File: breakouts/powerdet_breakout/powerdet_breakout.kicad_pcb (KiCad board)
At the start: 4 copper layers, 27.8 x 24 mm, 27 parts, among them P1 CONN_01X08, U1 CONN_SMA, U2 ADL5902, U3 CONN_SMA, U4 mounting_box

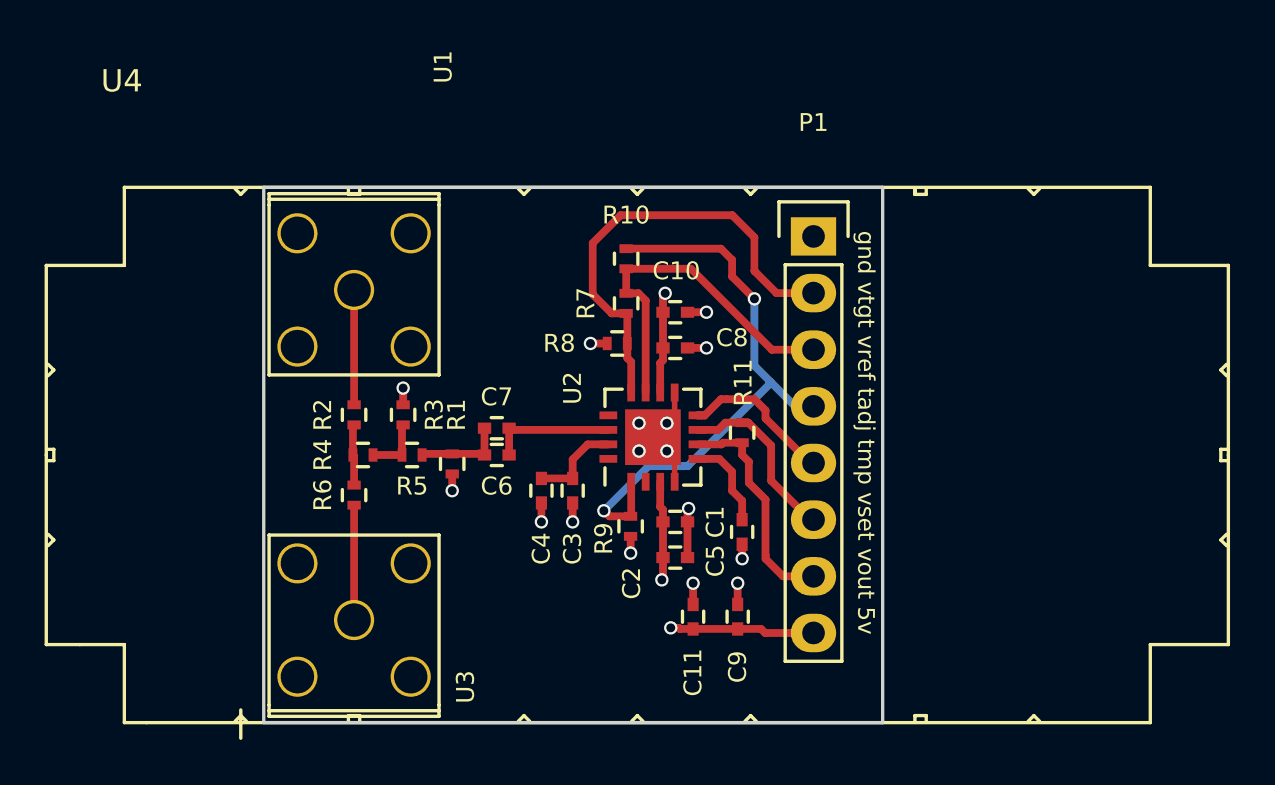
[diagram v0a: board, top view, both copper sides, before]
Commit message: trimmed ground plane on some breakouts so it doesn't disappear during panelization..
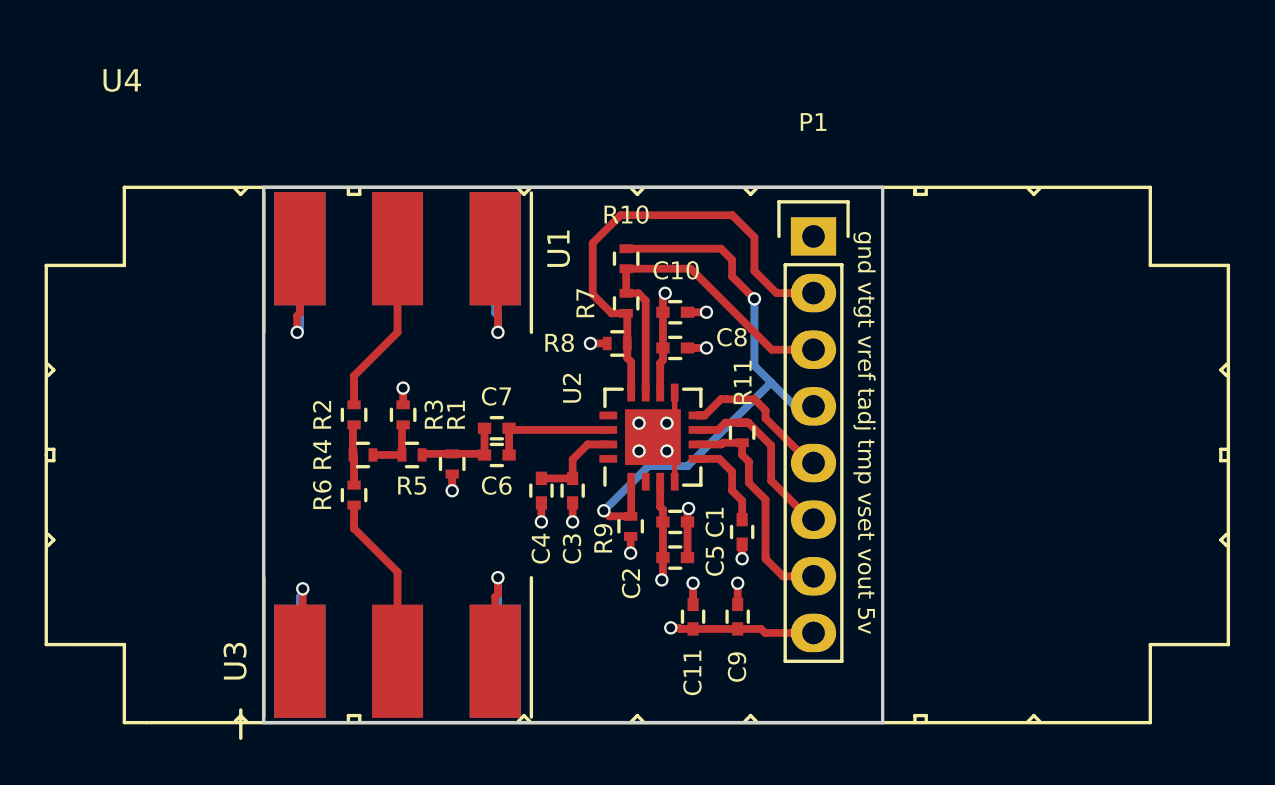
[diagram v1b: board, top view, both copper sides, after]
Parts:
- C11, C3, C7: value 1 nF -> 100 nF
- C2, C8: value 100 pF -> 30 pF
- C4, C6: value 1 nF -> 30 pF
- U1, U3: footprint vna_footprints:732512200_SMA -> vna_footprints:732511150_sma
- moved U1 2.69 mm to (137.8, 95.8), turned to 180 degrees
- moved U3 2.69 mm to (137.8, 114.2), turned to 0 degrees
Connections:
- U2 pad 13: Net-(U2-Pad13) -> (no net)
- U2 pad 16: Net-(U2-Pad16) -> (no net)
- U2 pad 2: Net-(U2-Pad2) -> (no net)
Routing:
- net GND: track 19.8 -> 49.2 mm, vias 16 -> 20
- net Net-(R6-Pad1): track 5.15 -> 7.81 mm
- net Net-(R2-Pad2): track 5.15 -> 7.81 mm
